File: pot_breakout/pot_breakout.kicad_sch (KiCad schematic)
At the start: 6 parts, among them J1 Conn_01x03, J2 Conn_01x03

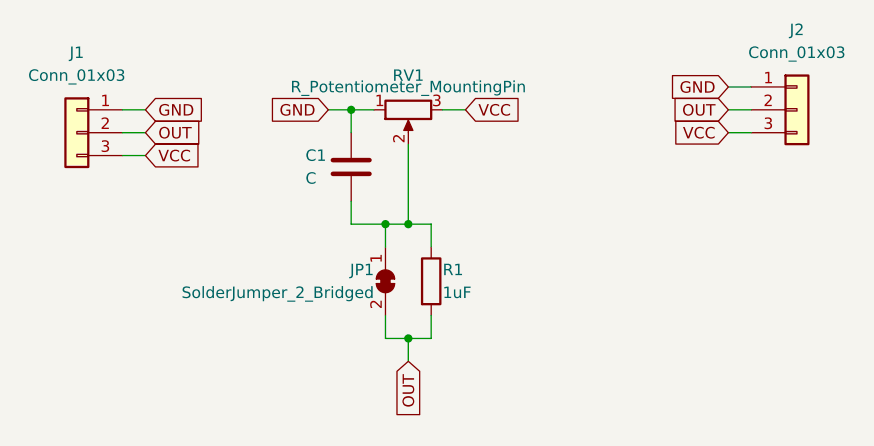
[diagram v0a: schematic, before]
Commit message: Added bike light.
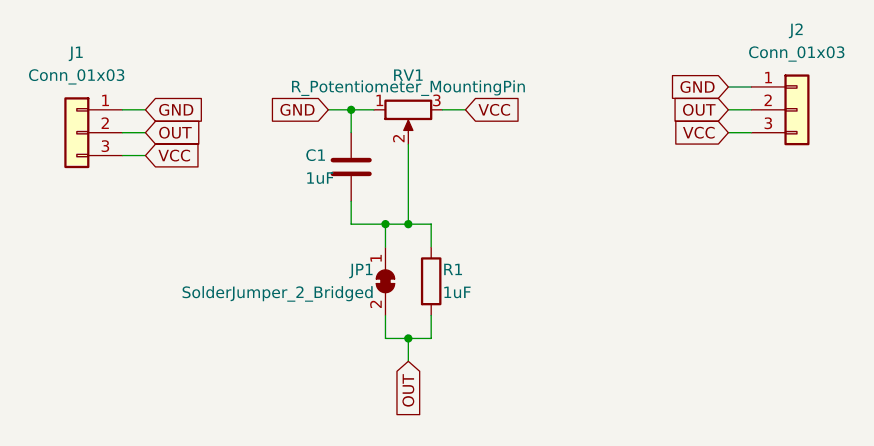
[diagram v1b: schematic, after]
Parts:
- C1: value C -> 1uF
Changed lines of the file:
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@@
       (effects (font (size 1.27 1.27)) (justify left))
     )
-    (property "Value" "C" (at 116.84 67.31 0)
+    (property "Value" "1uF" (at 116.84 67.31 0)
       (effects (font (size 1.27 1.27)) (justify left))
     )
